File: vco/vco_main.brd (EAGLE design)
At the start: 94.9 x 107.9 mm, 101 parts, among them IC1 OPA4130U, IC2 LM13700M, IC3 OPA4130U, IC4 OPA4130U, Q1 MMBFJ3

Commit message: did some stuff
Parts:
- moved R50 1.80 mm to (91.4, 14.0)
- moved R14 1.27 mm to (50.8, 71.1)
- moved R17 1.27 mm to (45.7, 71.1)
- moved R18 1.27 mm to (48.3, 71.1)
- moved R36 1.27 mm to (78.7, 39.4)
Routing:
- net SYNC: track 238.7 -> 235.7 mm, vias 13 -> 12
- net N$54: track 180.3 -> 177.5 mm
- net TRI: track 152.0 -> 150.5 mm
- net N$9: track 50.9 -> 52.2 mm
- net N$21: track 8.66 -> 7.39 mm
- net N$20: track 8.70 -> 7.43 mm
- net -12V: track 361.9 -> 363.2 mm
- net N$8: track 8.62 -> 7.39 mm
- net N$33: track 70.6 -> 69.7 mm
- net TOSQU: track 89.5 -> 88.9 mm
- net N$46: vias 4 -> 3
- net GND: vias 64 -> 67

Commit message: fixed some stuff
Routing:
- net SYNC: track 235.7 -> 233.5 mm, vias 12 -> 11
- net N$5: track 184.5 -> 183.0 mm
- net N$54: track 177.5 -> 176.5 mm
- net -12V: track 363.2 -> 364.2 mm
- net N$52: track 75.4 -> 76.4 mm
- net GND: vias 67 -> 69

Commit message: made some major layout changes.
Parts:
- moved U$6 32.2 mm to (45.7, 58.4)
- moved R48 32.0 mm to (49.5, 57.1)
- moved R19 28.0 mm to (52.1, 57.1)
- moved R28 26.7 mm to (68.6, 63.5)
- moved LINMODAMT 10.2 mm to (48.3, 44.5)
- moved SCALE 6.35 mm to (58.4, 40.6)
- moved R25 4.02 mm to (55.9, 35.6)
- moved R46 2.54 mm to (73.7, 39.4)
- moved R45 1.80 mm to (64.8, 38.1)
- moved R24 1.27 mm to (53.3, 64.8)
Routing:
- net N$25: track 46.6 -> 10.8 mm, vias 6 -> 0
- net N$22: track 37.7 -> 6.03 mm, vias 6 -> 0
- net -12V: track 364.2 -> 346.8 mm
- net N$5: track 183.0 -> 199.2 mm, vias 16 -> 17
- net +12V: track 268.0 -> 254.1 mm, vias 20 -> 19
- net N$24: track 52.7 -> 42.5 mm
- net N$46: track 34.1 -> 44.2 mm, vias 3 -> 2
- net N$10: track 37.0 -> 47.1 mm, vias 4 -> 3
- net N$56: track 38.3 -> 30.0 mm
- net N$55: track 79.6 -> 86.9 mm
- net N$51: track 90.2 -> 84.8 mm, vias 9 -> 6
- net TRI: track 150.5 -> 148.3 mm
- net SYNC: track 233.5 -> 232.0 mm
- net N$42: track 8.44 -> 7.39 mm
- net N$40: track 80.0 -> 79.0 mm
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
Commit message: made major layout changes
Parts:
- moved R21 80.0 mm to (7.62, 40.6)
- moved R9 58.5 mm to (10.2, 40.6)
- moved R25 21.3 mm to (62.2, 55.9), turned to 90 degrees
- moved SCALE 6.35 mm to (58.4, 47.0)
- moved R45 2.84 mm to (62.2, 36.8)
- moved R33 2.54 mm to (35.6, 57.1)
- moved R12 1.27 mm to (22.9, 40.6)
- moved R15 1.27 mm to (25.4, 40.6)
- moved R16 1.27 mm to (20.3, 40.6)
- moved R36 1.27 mm to (78.7, 40.6)
- moved R46 1.27 mm to (73.7, 40.6)
- moved R5 1.27 mm to (5.08, 40.6)
- moved C2 1.27 mm to (38.1, 73.7), turned to 270 degrees
- moved R14 1.27 mm to (50.8, 72.4)
- moved R17 1.27 mm to (45.7, 72.4)
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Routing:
- net SYNC: track 232.0 -> 74.1 mm, vias 11 -> 3
- net TRI: track 148.3 -> 213.5 mm, vias 10 -> 12
- net N$10: track 47.1 -> 17.5 mm, vias 3 -> 2
- net N$55: track 86.9 -> 80.6 mm
- net N$56: track 30.0 -> 24.4 mm
- net N$40: track 79.0 -> 74.9 mm, vias 4 -> 2
- net N$50: track 117.9 -> 114.9 mm
- net -12V: track 346.8 -> 344.2 mm
- net N$31: track 6.77 -> 9.31 mm
- net N$45: track 102.0 -> 99.8 mm
- net N$5: track 199.2 -> 197.2 mm, vias 17 -> 15
- net N$42: track 7.39 -> 6.12 mm
- net N$18: track 7.39 -> 6.12 mm
- net N$17: track 7.43 -> 6.16 mm
- net N$16: track 7.43 -> 6.16 mm
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
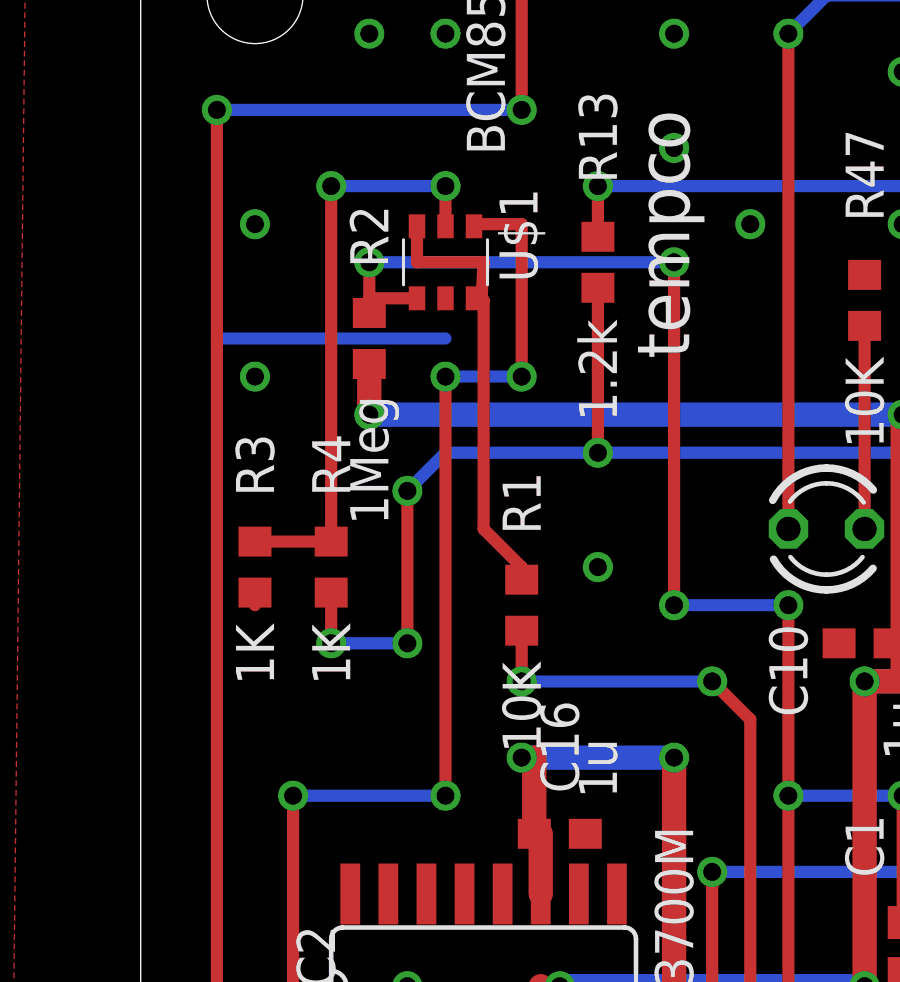
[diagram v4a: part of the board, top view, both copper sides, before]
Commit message: flipped the pnp pair right side up in schematic.
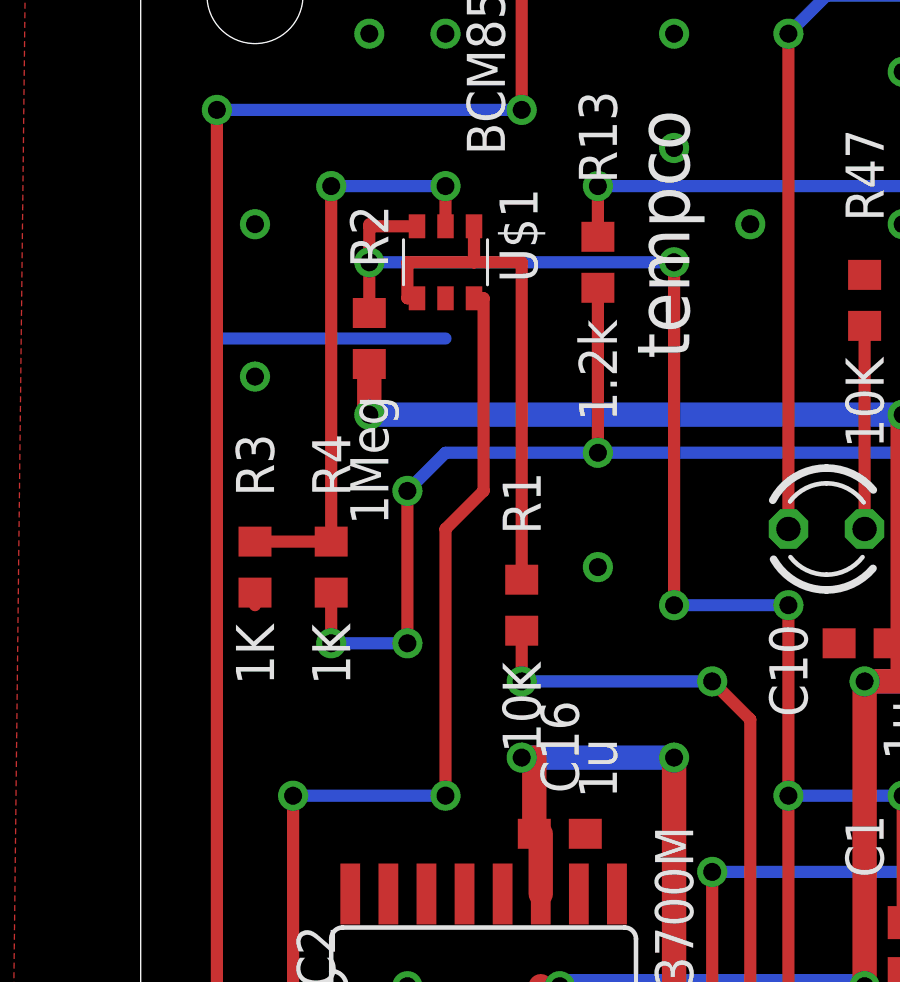
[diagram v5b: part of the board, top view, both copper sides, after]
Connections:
- removed net N$1: R1.2, U$1.3, U$1.6
- new net N$12: R1.2, U$1.1, U$1.4
- net IABC: now also U$1.6; no longer U$1.1
- net N$3: now also U$1.3; no longer U$1.4
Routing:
- net N$12: track 0.00 -> 17.1 mm
- net N$1: track 14.9 -> 0.00 mm
- net IABC: track 38.9 -> 33.1 mm, vias 4 -> 2
- net N$3: track 66.3 -> 67.6 mm

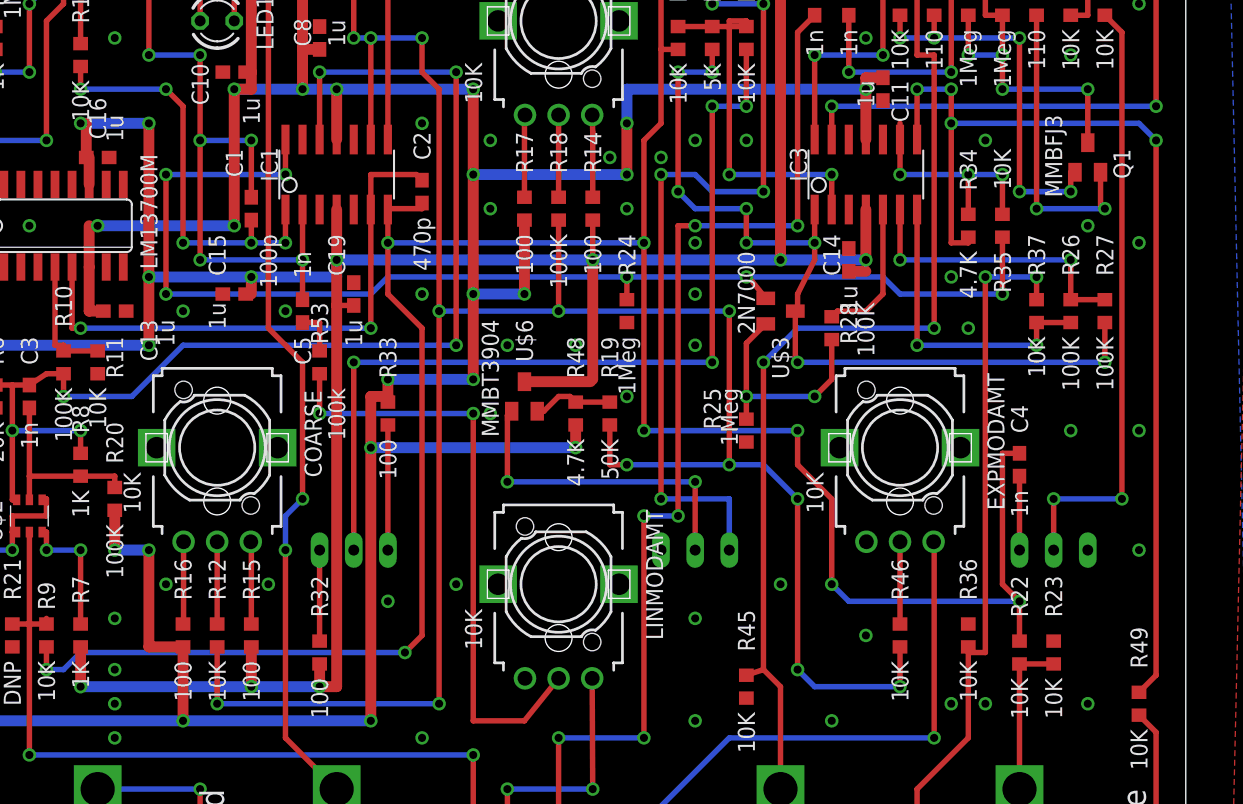
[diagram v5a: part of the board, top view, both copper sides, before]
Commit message: added a vcf schematic
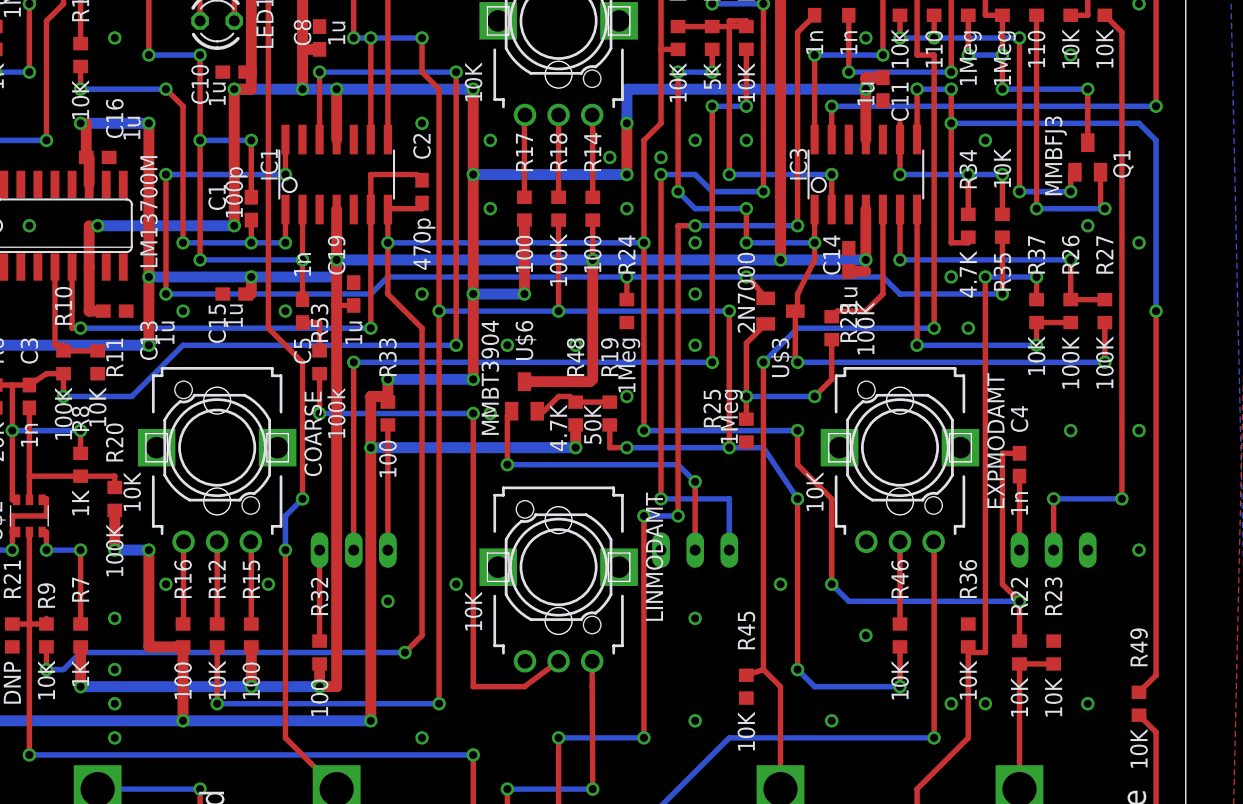
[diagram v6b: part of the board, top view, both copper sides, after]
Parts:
- moved LINMODAMT 1.27 mm to (48.3, 45.7)
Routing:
- net N$46: track 45.1 -> 41.7 mm
- net N$5: track 197.2 -> 195.6 mm
- net N$24: track 42.5 -> 43.8 mm
- net N$56: track 24.4 -> 23.7 mm
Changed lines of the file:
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@@
 </element>
 <element name="C1" library="dan" package="C0603" value="100p" x="25.4" y="72.39" smashed="yes" rot="R270">
-<attribute name="NAME" x="23.495" y="76.835" size="1.27" layer="21" font="vector" ratio="15" rot="R270"/>
-<attribute name="VALUE" x="26.035" y="70.485" size="1.27" layer="21" font="vector" ratio="15" rot="R270"/>
+<attribute name="NAME" x="22.225" y="74.295" size="1.27" layer="21" font="vector" ratio="15" rot="R270"/>
+<attribute name="VALUE" x="23.495" y="75.565" size="1.27" layer="21" font="vector" ratio="15" rot="R270"/>
 </element>
 <element name="FINE" library="dan" package="EVUFXJ" value="10K" x="48.26" y="86.36" smashed="yes">
@@
 <element name="R19" library="dan" package="R0603" value="50K" x="52.07" y="57.15" smashed="yes" rot="R90">
 <attribute name="NAME" x="51.435" y="62.865" size="1.27" layer="21" font="vector" ratio="15" rot="R270"/>
-<attribute name="VALUE" x="51.435" y="55.245" size="1.27" layer="21" font="vector" ratio="15" rot="R270"/>
+<attribute name="VALUE" x="50.165" y="57.785" size="1.27" layer="21" font="vector" ratio="15" rot="R270"/>
 </element>
 <element name="SCALE" library="dan" package="B64Y" value="" x="58.42" y="46.99" smashed="yes" rot="MR0">
@@
 </element>
 <element name="LINMOD" library="dan" package="PJ301BM" value="PJ301BM" x="31.75" y="8.89" smashed="yes"/>
-<element name="LINMODAMT" library="dan" package="EVUFXJ" value="10K" x="48.26" y="44.45" smashed="yes">
-<attribute name="NAME" x="54.76" y="49.99" size="1.27" layer="21" font="vector" ratio="15" rot="R270"/>
-<attribute name="VALUE" x="41.3" y="42.6" size="1.27" layer="21" font="vector" ratio="15" rot="R270"/>
+<element name="LINMODAMT" library="dan" package="EVUFXJ" value="10K" x="48.26" y="45.72" smashed="yes">
+<attribute name="NAME" x="54.76" y="51.26" size="1.27" layer="21" font="vector" ratio="15" rot="R270"/>
+<attribute name="VALUE" x="41.3" y="43.87" size="1.27" layer="21" font="vector" ratio="15" rot="R270"/>
 </element>
 <element name="SYNC" library="dan" package="PJ301BM" value="PJ301BM" x="31.75" y="24.13" smashed="yes"/>
@@
 <element name="C10" library="dan" package="C0603" value="1u" x="24.13" y="82.55" smashed="yes" rot="R180">
 <attribute name="NAME" x="20.955" y="83.185" size="1.27" layer="21" font="vector" ratio="15" rot="R270"/>
-<attribute name="VALUE" x="24.765" y="80.645" size="1.27" layer="21" font="vector" ratio="15" rot="R270"/>
+<attribute name="VALUE" x="22.225" y="81.915" size="1.27" layer="21" font="vector" ratio="15" rot="R270"/>
 </element>
 <element name="C11" library="dan" package="C0603" value="1u" x="72.39" y="81.28" smashed="yes" rot="R270">
@@
 </element>
 <element name="C15" library="dan" package="C0603" value="1u" x="24.13" y="66.04" smashed="yes" rot="R180">
-<attribute name="NAME" x="22.225" y="70.485" size="1.27" layer="21" font="vector" ratio="15" rot="R270"/>
-<attribute name="VALUE" x="22.225" y="65.405" size="1.27" layer="21" font="vector" ratio="15" rot="R270"/>
+<attribute name="NAME" x="22.225" y="65.405" size="1.27" layer="21" font="vector" ratio="15" rot="R270"/>
+<attribute name="VALUE" x="23.495" y="65.405" size="1.27" layer="21" font="vector" ratio="15" rot="R270"/>
 </element>
 <element name="C16" library="dan" package="C0603" value="1u" x="13.97" y="76.2" smashed="yes">
-<attribute name="NAME" x="13.335" y="80.645" size="1.27" layer="21" font="vector" ratio="15" rot="R270"/>
-<attribute name="VALUE" x="14.605" y="79.375" size="1.27" layer="21" font="vector" ratio="15" rot="R270"/>
+<attribute name="NAME" x="14.605" y="80.645" size="1.27" layer="21" font="vector" ratio="15" rot="R270"/>
+<attribute name="VALUE" x="15.875" y="79.375" size="1.27" layer="21" font="vector" ratio="15" rot="R270"/>
 </element>
 <element name="C17" library="dan" package="C0603" value="1u" x="45.72" y="102.87" smashed="yes" rot="R180">
@@
 <element name="R48" library="dan" package="R0603" value="4.7K" x="49.53" y="57.15" smashed="yes" rot="R90">
 <attribute name="NAME" x="48.895" y="62.865" size="1.27" layer="21" font="vector" ratio="15" rot="R270"/>
-<attribute name="VALUE" x="48.895" y="55.245" size="1.27" layer="21" font="vector" ratio="15" rot="R270"/>
+<attribute name="VALUE" x="47.625" y="57.785" size="1.27" layer="21" font="vector" ratio="15" rot="R270"/>
 </element>
 <element name="R49" library="dan" package="R0603" value="10K" x="91.44" y="35.56" smashed="yes" rot="R270">
@@
 <wire x1="48.26" y1="64.77" x2="60.96" y2="64.77" width="0.4064" layer="16"/>
 <via x="60.96" y="64.77" extent="1-16" drill="0.6" shape="square"/>
-<wire x1="60.96" y1="64.77" x2="60.96" y2="53.34" width="0.4064" layer="1"/>
-<via x="60.96" y="53.34" extent="1-16" drill="0.6" shape="square"/>
+<wire x1="60.96" y1="64.77" x2="60.96" y2="54.61" width="0.4064" layer="1"/>
+<via x="60.96" y="54.61" extent="1-16" drill="0.6" shape="square"/>
 <via x="66.04" y="50.8" extent="1-16" drill="0.6" shape="square"/>
 <wire x1="66.04" y1="50.8" x2="66.04" y2="38.1" width="0.4064" layer="1"/>
@@
 <wire x1="38.1" y1="82.55" x2="39.37" y2="81.28" width="0.4064" layer="1"/>
 <wire x1="39.37" y1="81.28" x2="39.37" y2="64.77" width="0.4064" layer="1"/>
-<wire x1="52.07" y1="56.3" x2="52.07" y2="53.34" width="0.4064" layer="1"/>
-<wire x1="52.07" y1="53.34" x2="53.34" y2="53.34" width="0.4064" layer="1"/>
-<via x="53.34" y="53.34" extent="1-16" drill="0.6" shape="square"/>
-<wire x1="53.34" y1="53.34" x2="60.96" y2="53.34" width="0.4064" layer="16"/>
-<wire x1="66.04" y1="50.8" x2="63.5" y2="53.34" width="0.4064" layer="16"/>
-<wire x1="63.5" y1="53.34" x2="60.96" y2="53.34" width="0.4064" layer="16"/>
+<wire x1="52.07" y1="56.3" x2="52.07" y2="54.61" width="0.4064" layer="1"/>
+<wire x1="52.07" y1="54.61" x2="53.34" y2="54.61" width="0.4064" layer="1"/>
+<via x="53.34" y="54.61" extent="1-16" drill="0.6" shape="square"/>
+<wire x1="53.34" y1="54.61" x2="60.96" y2="54.61" width="0.4064" layer="16"/>
+<wire x1="66.04" y1="50.8" x2="63.5" y2="54.61" width="0.4064" layer="16"/>
+<wire x1="63.5" y1="54.61" x2="60.96" y2="54.61" width="0.4064" layer="16"/>
 <wire x1="66.04" y1="38.1" x2="67.31" y2="36.83" width="0.4064" layer="16"/>
 <wire x1="67.31" y1="36.83" x2="73.66" y2="36.83" width="0.4064" layer="16"/>
@@
 <via x="77.47" y="78.74" extent="1-16" drill="0.6" shape="square"/>
 <wire x1="77.47" y1="78.74" x2="91.44" y2="78.74" width="0.4064" layer="16"/>
-<wire x1="91.44" y1="78.74" x2="92.71" y2="77.47" width="0.4064" layer="16"/>
-<via x="92.71" y="77.47" extent="1-16" drill="0.6" shape="square"/>
-<wire x1="92.71" y1="77.47" x2="92.71" y2="37.68" width="0.4064" layer="1"/>
+<via x="92.71" y="64.77" extent="1-16" drill="0.6" shape="square"/>
+<wire x1="92.71" y1="64.77" x2="92.71" y2="37.68" width="0.4064" layer="1"/>
 <contactref element="R49" pad="1"/>
 <wire x1="91.44" y1="36.41" x2="92.71" y2="37.68" width="0.4064" layer="1"/>
+<wire x1="92.71" y1="64.77" x2="92.71" y2="77.47" width="0.4064" layer="16"/>
+<wire x1="92.71" y1="77.47" x2="91.44" y2="78.74" width="0.4064" layer="16"/>
 </signal>
 <signal name="N$33">
@@
 <wire x1="58.42" y1="46.99" x2="58.42" y2="52.07" width="0.4064" layer="1"/>
 <via x="58.42" y="52.07" extent="1-16" drill="0.6" shape="square"/>
-<wire x1="58.42" y1="52.07" x2="44.45" y2="52.07" width="0.4064" layer="16"/>
-<via x="44.45" y="52.07" extent="1-16" drill="0.6" shape="square"/>
-<wire x1="44.45" y1="52.07" x2="44.45" y2="57" width="0.4064" layer="1"/>
+<via x="44.45" y="53.34" extent="1-16" drill="0.6" shape="square"/>
+<wire x1="44.45" y1="53.34" x2="44.45" y2="57" width="0.4064" layer="1"/>
 <wire x1="44.45" y1="57" x2="44.77" y2="57.32" width="0.4064" layer="1"/>
+<wire x1="58.42" y1="52.07" x2="57.15" y2="53.34" width="0.4064" layer="16"/>
+<wire x1="57.15" y1="53.34" x2="44.45" y2="53.34" width="0.4064" layer="16"/>
 </signal>
 <signal name="N$57">
@@
 <via x="50.8" y="29.21" extent="1-16" drill="0.6" shape="square"/>
 <wire x1="50.8" y1="29.21" x2="50.76" y2="36.83" width="0.4064" layer="1"/>
-<wire x1="50.76" y1="36.83" x2="50.76" y2="37.45" width="0.4064" layer="1"/>
+<wire x1="50.76" y1="36.83" x2="50.76" y2="38.72" width="0.4064" layer="1"/>
 <wire x1="44.45" y1="13.97" x2="31.75" y2="13.97" width="0.4064" layer="16"/>
 </signal>
@@
 <wire x1="30.48" y1="57.15" x2="41.91" y2="57.15" width="0.4064" layer="16"/>
 <via x="41.91" y="57.15" extent="1-16" drill="0.6" shape="square"/>
-<wire x1="41.91" y1="57.15" x2="41.91" y2="34.29" width="0.4064" layer="1"/>
-<wire x1="48.26" y1="37.45" x2="45.72" y2="34.29" width="0.4064" layer="1"/>
-<wire x1="45.72" y1="34.29" x2="41.91" y2="34.29" width="0.4064" layer="1"/>
+<wire x1="41.91" y1="57.15" x2="41.91" y2="36.83" width="0.4064" layer="1"/>
+<wire x1="48.26" y1="38.72" x2="45.72" y2="36.83" width="0.4064" layer="1"/>
+<wire x1="45.72" y1="36.83" x2="41.91" y2="36.83" width="0.4064" layer="1"/>
 </signal>
 <signal name="N$48">
